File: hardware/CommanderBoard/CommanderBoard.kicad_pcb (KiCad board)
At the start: 2 copper layers, 81.3 x 106.7 mm, 37 parts, among them J1 Conn_01x22, J1BUS1 Conn_02x04_Odd_Even, J1BUS2 Conn_02x04_Odd_Even, J2 Conn_01x22, J2BUS1 Conn_01x02, J2BUS2 Conn_01x02, J3 HUB75, SW1 SW_SPDT, SW2 SW_DP3T, SW3 SW_DP3T, SW4 SW_DPDT_x2

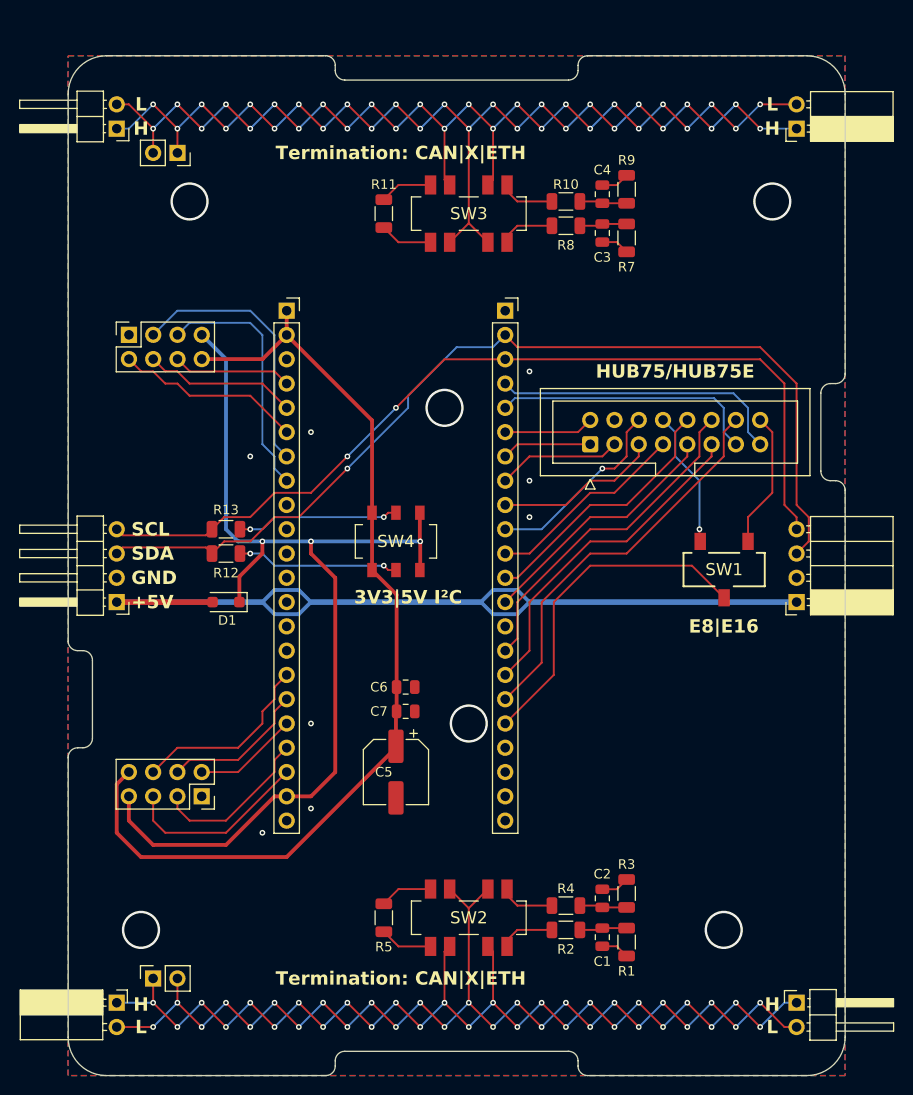
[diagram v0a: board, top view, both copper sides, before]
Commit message: Reworked Commanderboard, horizontal orientation of the ESP32-S3.
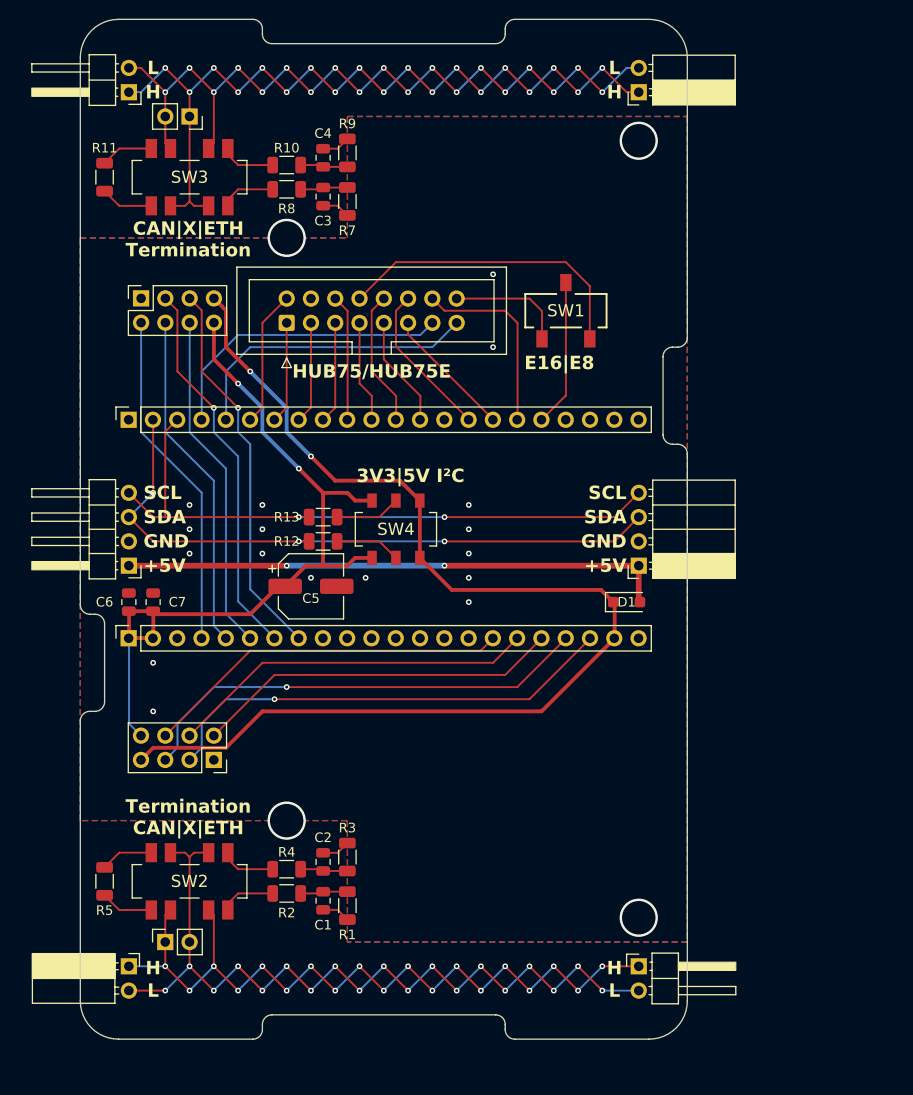
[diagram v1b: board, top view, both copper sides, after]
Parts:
- moved D1 41.9 mm to (152.4, 83.8), turned to 0 degrees
- moved J1 41.0 mm to (100.3, 64.7), turned to 90 degrees
- moved J2 38.0 mm to (100.3, 87.6), turned to 90 degrees
- moved J3 34.2 mm to (116.8, 54.6)
- moved SW1 31.7 mm to (146.1, 53.3), turned to 0 degrees
- moved C6 30.3 mm to (100.3, 83.8), turned to -90 degrees
- moved C1 29.5 mm to (120.7, 115.1)
- moved C2 29.5 mm to (120.7, 111.0)
- moved C3 29.5 mm to (120.7, 41.4)
- moved C4 29.5 mm to (120.7, 37.3)
- moved R1 29.5 mm to (123.2, 115.6)
- moved R10 29.5 mm to (116.8, 38.1)
- moved R2 29.5 mm to (116.8, 114.3)
- moved R3 29.5 mm to (123.2, 110.5)
- moved R4 29.5 mm to (116.8, 111.8)
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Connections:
- J1 pad 4: H75_OE -> H75_CLK
- J1 pad 5: H75_CLK -> H75_OE
- J2 pad 19: RxD1/MOSI1 -> TxD1/MISO1
- J2 pad 20: TxD1/MISO1 -> RxD1/MOSI1
- J2 pad 4: CS_N2 -> IRQ_N2
- J2 pad 6: IRQ_N2 -> CS_N2
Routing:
- net +5VEXT: track 95.5 -> 57.0 mm, vias 0 -> 2
- net I2C_SDA: track 102.8 -> 67.8 mm, vias 1 -> 3
- net RxD1/MOSI1: track 17.1 -> 48.7 mm, vias 0 -> 1
- net TxD1/MISO1: track 19.7 -> 48.7 mm, vias 0 -> 1
- net BUS1H: track 113.2 -> 84.5 mm, vias 26 -> 19
- net BUS1L: track 116.6 -> 88.1 mm, vias 26 -> 19
- net IRQ_N1: track 11.0 -> 38.6 mm
- net I2C_SCL: track 94.6 -> 67.3 mm
- net BUS2L: track 113.2 -> 86.6 mm, vias 26 -> 19
- net BUS2H: track 116.6 -> 90.2 mm, vias 26 -> 19
- net SCLK1: track 15.3 -> 38.6 mm
- net CS_N2: track 12.5 -> 35.6 mm
- net H75_C: track 35.3 -> 13.8 mm
- net H75_LAT: track 41.4 -> 20.1 mm
- net +3V3: track 102.8 -> 81.7 mm, vias 0 -> 2
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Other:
- board size 81.3 x 106.7 mm -> 63.5 x 106.7 mm
- board text added: "CAN|X|ETH Termination"
- board text added: "E16|E8"
- board text added: "Termination CAN|X|ETH"
- board text removed: "E8|E16"
- board text removed: "Termination: CAN|X|ETH"

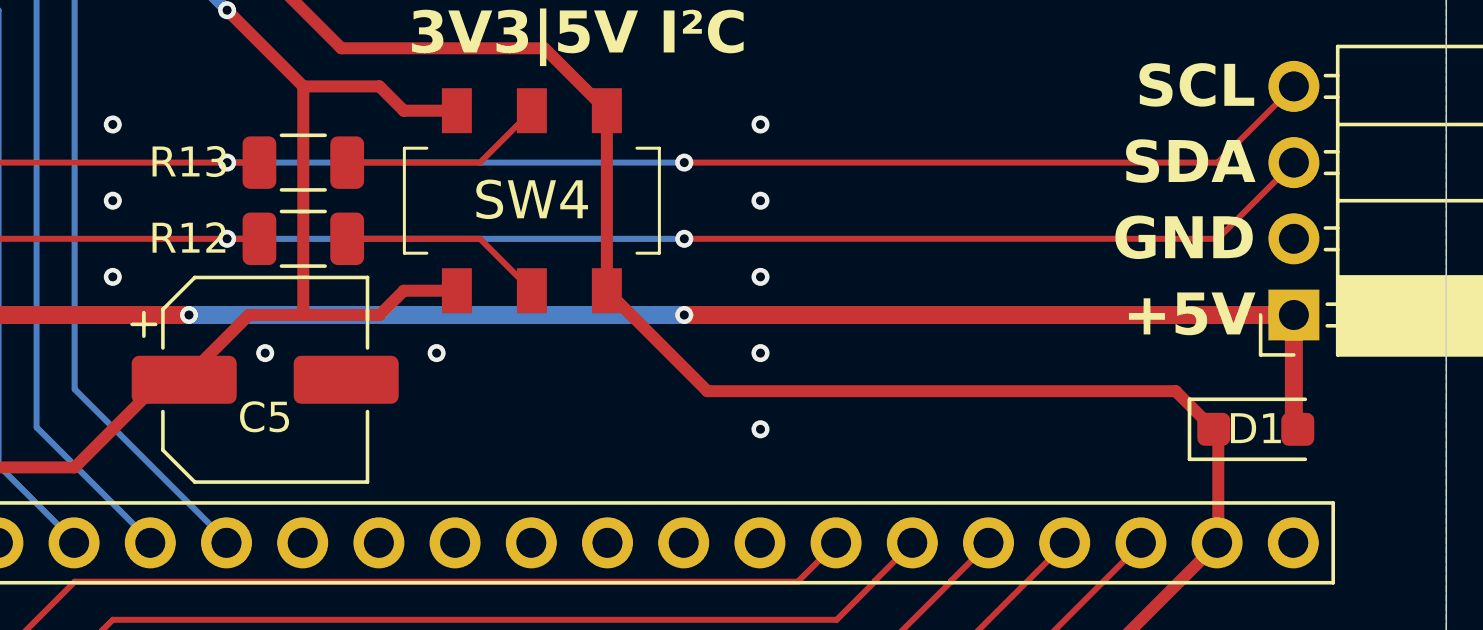
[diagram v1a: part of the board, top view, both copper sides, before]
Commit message: Updated step files for all boards, footprints for LINBoard.
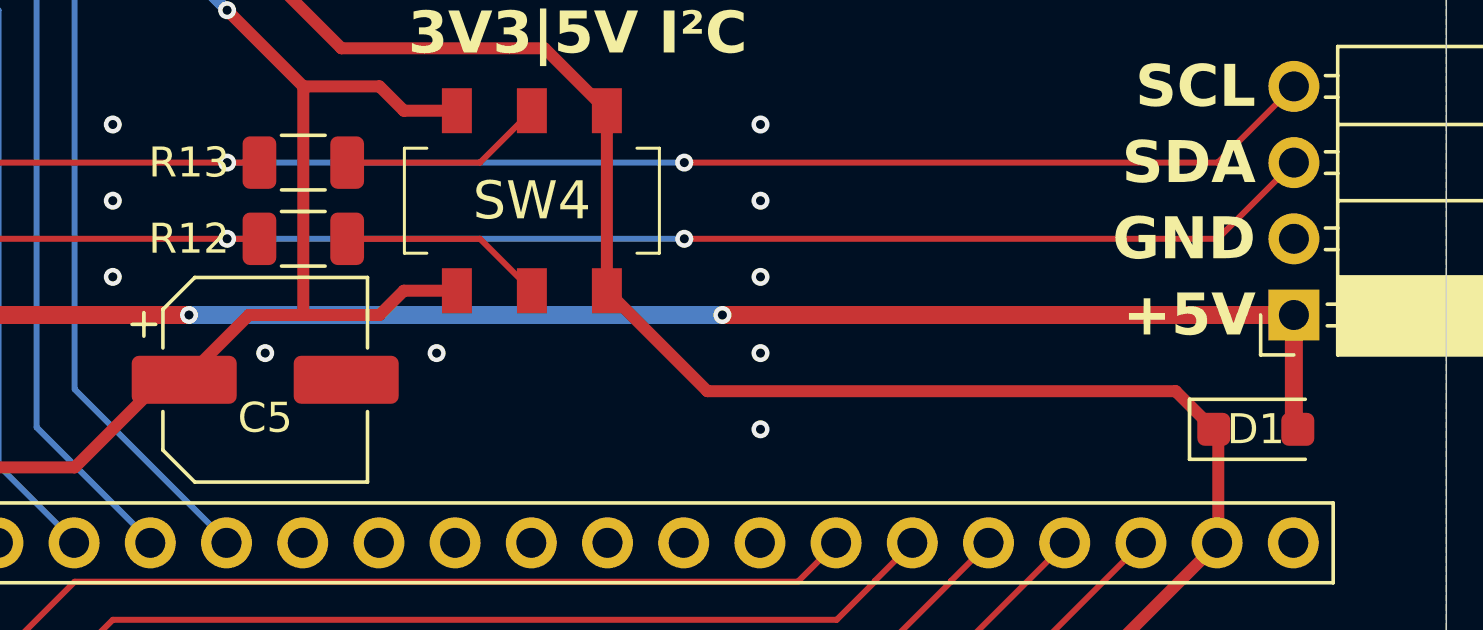
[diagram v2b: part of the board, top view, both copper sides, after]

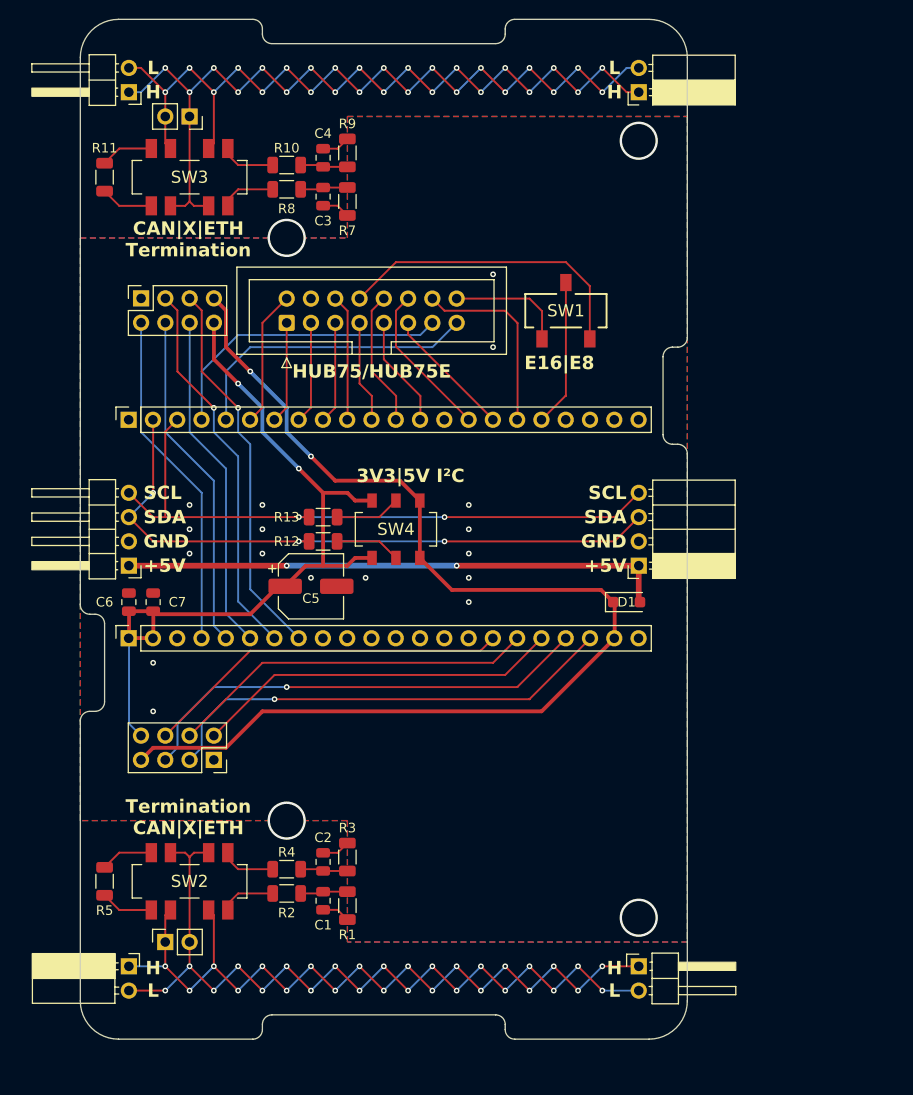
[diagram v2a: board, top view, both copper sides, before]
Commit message: Added two joysticks to CommanderBoard.
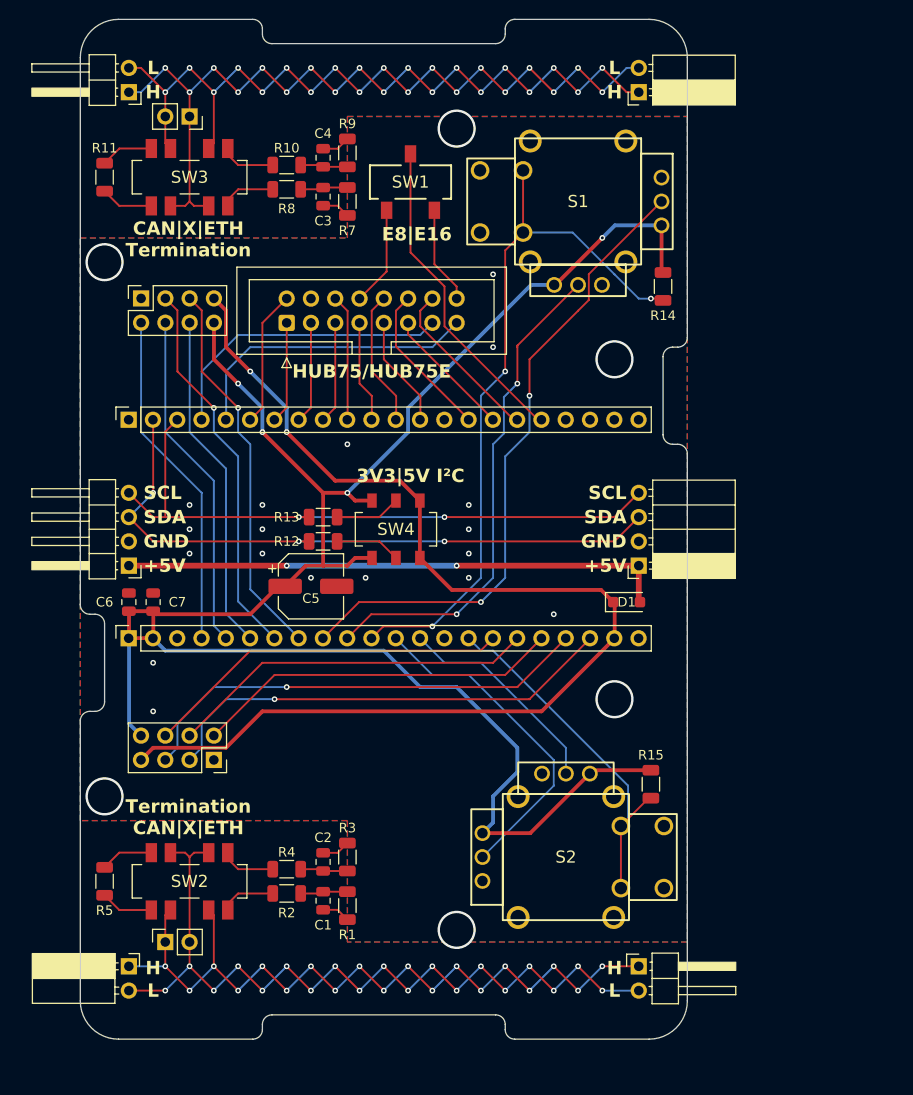
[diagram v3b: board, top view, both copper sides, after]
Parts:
- added R14: 10k, Resistor_SMD:R_1206_3216Metric, F.Cu at (156.2, 50.8)
- added R15: 10k, Resistor_SMD:R_1206_3216Metric, F.Cu at (154.9, 102.9)
- added S1: THB001P, LIB_THB001P:THB001P, F.Cu at (147.3, 41.9)
- added S2: THB001P, LIB_THB001P:THB001P, F.Cu at (146.1, 110.5)
- moved SW1 21.1 mm to (129.8, 39.9)
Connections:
- J2 pad 10: unconnected-(J2-Pin_10-Pad10) -> S1hCh
- J2 pad 11: unconnected-(J2-Pin_11-Pad11) -> BTN1
- J2 pad 12: unconnected-(J2-Pin_12-Pad12) -> S2vCh
- J2 pad 13: unconnected-(J2-Pin_13-Pad13) -> S2hCh
- J2 pad 15: unconnected-(J2-Pin_15-Pad15) -> BTN2
- J2 pad 9: unconnected-(J2-Pin_9-Pad9) -> S1vCh
- SW1 pad 1: H75_E16 -> H75_E8
- SW1 pad 3: H75_E8 -> H75_E16
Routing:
- net +3V3: track 81.7 -> 206.3 mm, vias 2 -> 4
- net BTN1: track 0.00 -> 76.1 mm, vias 0 -> 3
- net S1vCh: track 0.00 -> 67.8 mm, vias 0 -> 2
- net S1hCh: track 0.00 -> 52.2 mm, vias 0 -> 2
- net BTN2: track 0.00 -> 38.4 mm
- net S2vCh: track 0.00 -> 35.1 mm
- net S2hCh: track 0.00 -> 22.7 mm
- net H75_E8: track 32.2 -> 10.4 mm
- net H75_E: track 15.4 -> 33.7 mm
- net H75_LAT: track 20.1 -> 17.6 mm
- net H75_E16: track 12.4 -> 10.2 mm
- net GNDREF: vias 21 -> 24
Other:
- board text added: "E8|E16"
- board text removed: "E16|E8"

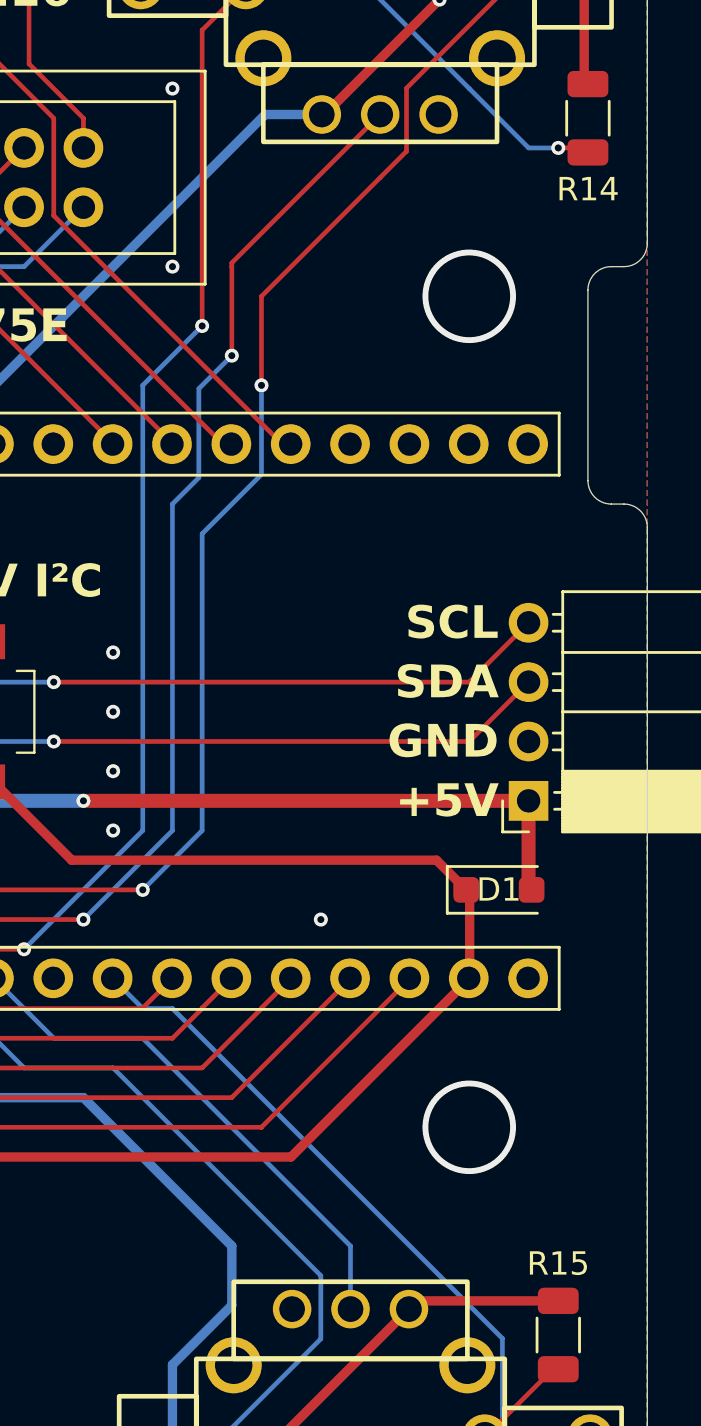
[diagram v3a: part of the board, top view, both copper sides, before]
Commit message: Added software for thumbstick test.
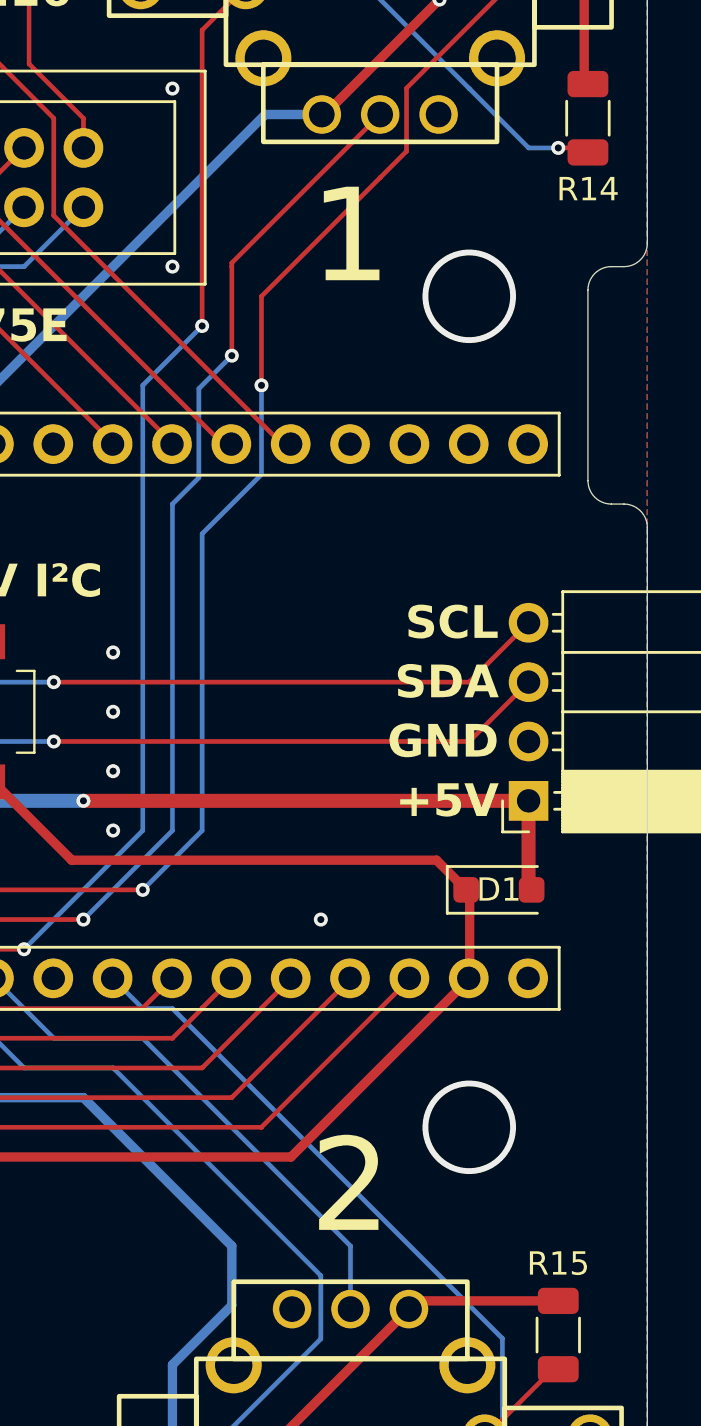
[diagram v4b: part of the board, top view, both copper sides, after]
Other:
- board text added: "1"
- board text added: "2"
- board text added: "COMChallange Commanderboard v1.1 github.com/raphweb"
- board text removed: "COMChallange Commanderboard v1.0 github.com/raphweb"
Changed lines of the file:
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@@
 		(layer "Edge.Cuts")
 	)
-	(gr_text "COMChallange\nCommanderboard v1.0\ngithub.com/raphweb"
+	(gr_text "COMChallange\nCommanderboard v1.1\ngithub.com/raphweb"
 		(at 125.73 103.632 0)
 		(layer "F.Mask")
@@
 		)
 	)
+	(gr_text "2"
+		(at 146.05 96.52 0)
+		(layer "F.SilkS")
+		(effects
+			(font
+				(face "Hack")
+				(size 4 4)
+				(thickness 0.254)
+			)
+		)
+		(render_cache "2" 0
+			(polygon
+				(pts
+					(xy 144.781403 97.813635) (xy 144.798697 97.720214) (xy 144.849791 97.644131) (xy 145.218842 97.254563)
+					(xy 145.675576 96.763635) (xy 145.955722 96.45882) (xy 146.099093 96.300307) (xy 146.200454 96.181116)
+					(xy 146.431508 95.88314) (xy 146.572436 95.639874) (xy 146.644598 95.42405) (xy 146.667935 95.213182)
+					(xy 146.643881 94.995561) (xy 146.576635 94.822058) (xy 146.468388 94.682686) (xy 146.322581 94.577788)
+					(xy 146.140981 94.512087) (xy 145.913468 94.488513) (xy 145.6788 94.508264) (xy 145.420572 94.570802)
+					(xy 145.133984 94.68264) (xy 144.814131 94.852191) (xy 144.814131 94.29434) (xy 145.095238 94.175822)
+					(xy 145.369295 94.092107) (xy 145.640222 94.040606) (xy 145.905164 94.023719) (xy 146.183462 94.043305)
+					(xy 146.438346 94.100411) (xy 146.672768 94.199496) (xy 146.873099 94.34099) (xy 147.019922 94.500759)
+					(xy 147.13566 94.695143) (xy 147.208698 94.913864) (xy 147.234089 95.166775) (xy 147.204724 95.432064)
+					(xy 147.113678 95.705331) (xy 147.045722 95.839227) (xy 146.959316 95.972044) (xy 146.717272 96.279546)
+					(xy 146.528472 96.495701) (xy 146.274215 96.774626) (xy 146.081508 96.977103) (xy 145.894173 97.164193)
+					(xy 145.668493 97.391095) (xy 145.358304 97.715205) (xy 147.261445 97.715205) (xy 147.261445 98.18)
+					(xy 144.781403 98.18)
+				)
+			)
+		)
+	)
 	(gr_text "3V3|5V I²C"
 		(at 129.794 70.612 0)
@@
 			)
 		)
+	)
+	(gr_text "1"
+		(at 146.05 55.88 0)
+		(layer "F.SilkS")
+		(effects
+			(font
+				(face "Hack")
+				(size 4 4)
+				(thickness 0.254)
+			)
+		)
+		(render_cache "1" 0
+			(polygon
+				(pts
+					(xy 145.104048 57.075205) (xy 145.962561 57.075205) (xy 145.962561 54.146734) (xy 145.311898 54.887766)
+					(xy 145.010991 54.521158) (xy 145.957188 53.45748) (xy 146.509421 53.45748) (xy 146.509421 57.075205)
+					(xy 147.357188 57.075205) (xy 147.357188 57.54) (xy 145.104048 57.54)
+				)
+			)
+		)
